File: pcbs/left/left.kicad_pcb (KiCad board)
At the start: 2 copper layers, 135.8 x 108.6 mm, 70 parts

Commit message: left pcb initial commit
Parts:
- moved D1 10.0 mm to (38.9, 144.1)
- moved D23 10.0 mm to (133.9, 106.6)
- moved S25 10.0 mm to (85.9, 152.6)
- moved S14 10.0 mm to (99.9, 114.6)
- moved S5 10.0 mm to (61.9, 138.1)
- moved S24 10.0 mm to (137.9, 81.6)
- moved S27 10.0 mm to (128.9, 157.6)
- moved D15 10.0 mm to (95.9, 101.6)
- moved H2 10.0 mm to (128.4, 87.3)
- moved D27 10.0 mm to (138.8, 163.3)
- moved S12 10.0 mm to (80.9, 78.6)
- moved MCU1 10.0 mm to (157.9, 92.6)
- moved H5 10.0 mm to (128.4, 140.5)
- moved CONN1 10.0 mm to (157.9, 81.6)
- moved D7 10.0 mm to (57.9, 106.1)
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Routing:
- net row0: track 0.00 -> 200.2 mm, vias 0 -> 2
- net row1: track 0.00 -> 186.4 mm, vias 0 -> 2
- net row2: track 0.00 -> 164.0 mm, vias 0 -> 2
- net col3: track 0.00 -> 150.8 mm, vias 0 -> 8
- net row3: track 0.00 -> 142.1 mm, vias 0 -> 2
- net col2: track 0.00 -> 141.1 mm, vias 0 -> 12
- net row4: track 0.00 -> 130.1 mm, vias 0 -> 2
- net col0: track 0.00 -> 125.7 mm, vias 0 -> 12
- net col1: track 0.00 -> 125.4 mm, vias 0 -> 12
- net row5: track 0.00 -> 123.3 mm
- net col4: track 0.00 -> 122.2 mm, vias 0 -> 3
- net layer_cluster: track 0.00 -> 19.5 mm
- net space_cluster: track 0.00 -> 19.5 mm
- net home_cluster: track 0.00 -> 19.5 mm
- net inner_cluster: track 0.00 -> 19.5 mm
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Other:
- outline, holes or cut-outs redrawn
- net class Default removed

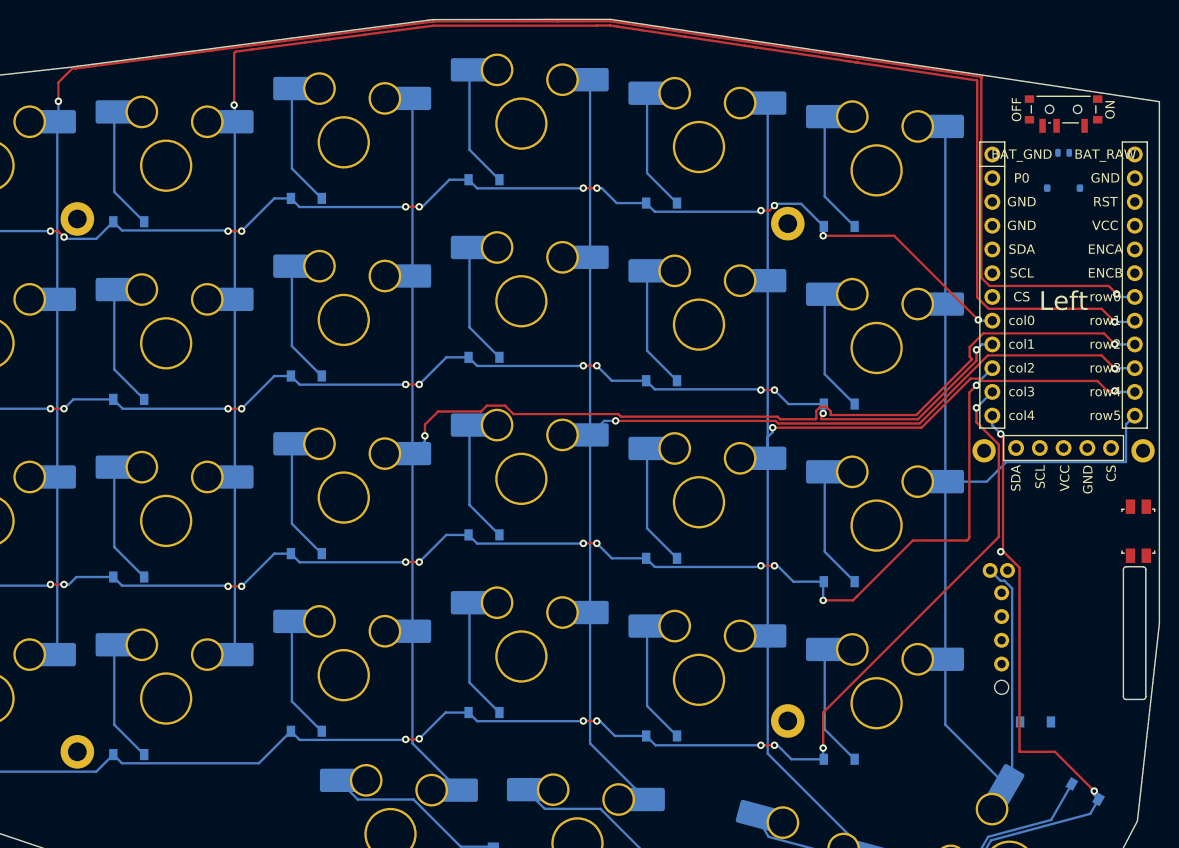
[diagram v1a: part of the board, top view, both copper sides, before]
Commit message: left and right mostly finished
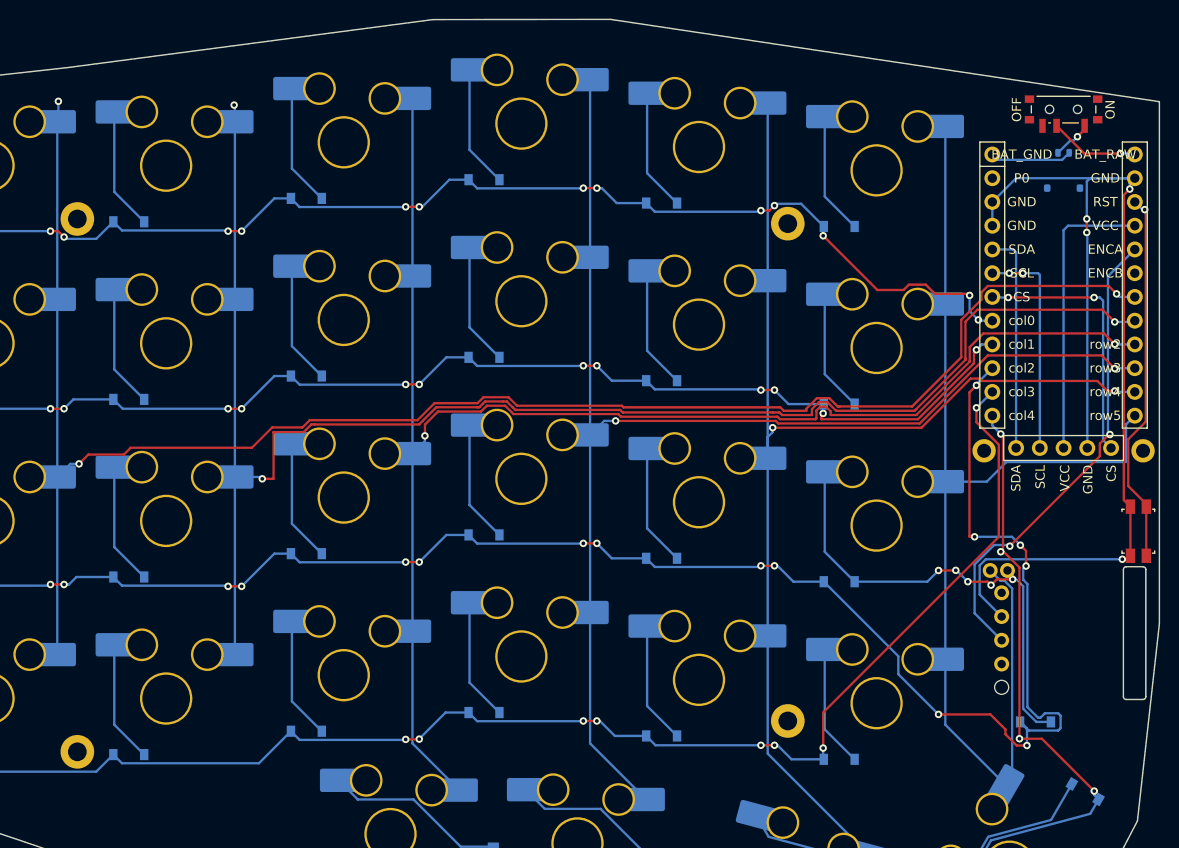
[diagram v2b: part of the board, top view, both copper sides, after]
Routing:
- net GND: track 0.00 -> 116.8 mm, vias 0 -> 4
- net ENCA: track 0.00 -> 51.5 mm, vias 0 -> 2
- net col2: track 141.1 -> 188.3 mm, vias 12 -> 16
- net RST: track 0.00 -> 40.0 mm, vias 0 -> 1
- net inner_home: track 13.1 -> 51.6 mm, vias 0 -> 5
- net VCC: track 0.00 -> 31.1 mm
- net CS: track 0.00 -> 28.1 mm, vias 0 -> 2
- net SCL: track 0.00 -> 23.7 mm, vias 0 -> 2
- net SDA: track 0.00 -> 23.6 mm
- net row1: track 186.4 -> 170.9 mm, vias 2 -> 3
- net row0: track 200.2 -> 188.3 mm, vias 2 -> 3
- net BAT_RAW: track 0.00 -> 9.64 mm, vias 0 -> 1
- net BAT_GND: track 0.00 -> 8.77 mm
- net ON_P: track 0.00 -> 4.28 mm, vias 0 -> 1
- net col0: track 125.7 -> 127.1 mm, vias 12 -> 13
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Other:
- board text removed: "Left"

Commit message: added fill
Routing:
- added copper zone on B.Cu, net (none)
- added copper zone on F.Cu, net (none)
